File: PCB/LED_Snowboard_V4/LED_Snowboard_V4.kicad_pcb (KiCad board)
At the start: 4 copper layers, 100 x 100 mm, 114 parts, among them J1 Charge_Balance, J10 Output, J11 Micro_SD_Card_Det_Hirose_DM3AT, J12 Power Switch, J2 Bat2_Balance, J3 Bat1_Balance, J4 Bat1, J5 Bat2, J7 LED Data, J8 Sensor Input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

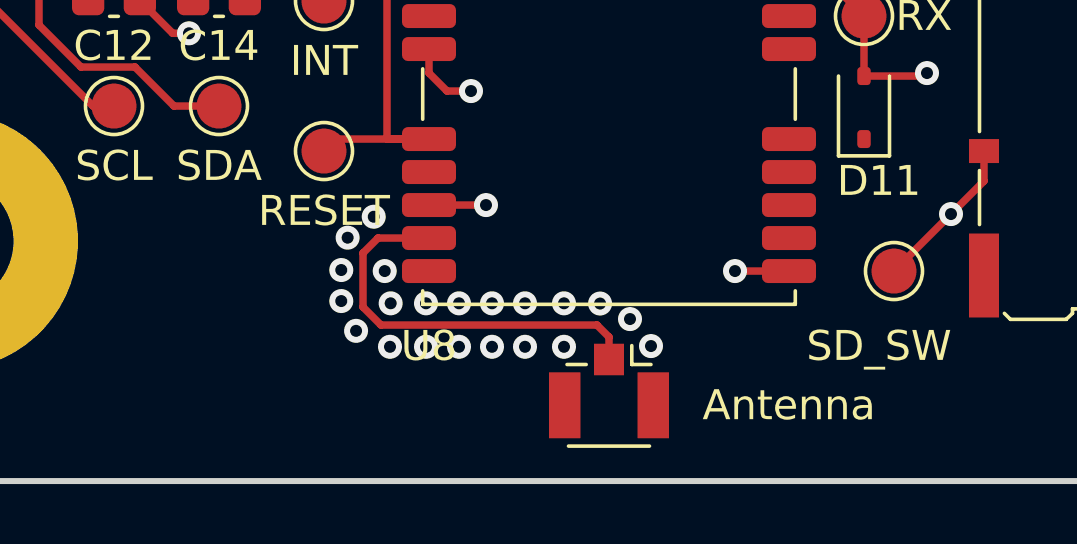
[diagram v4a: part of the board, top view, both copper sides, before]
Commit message: impedance matched antennae
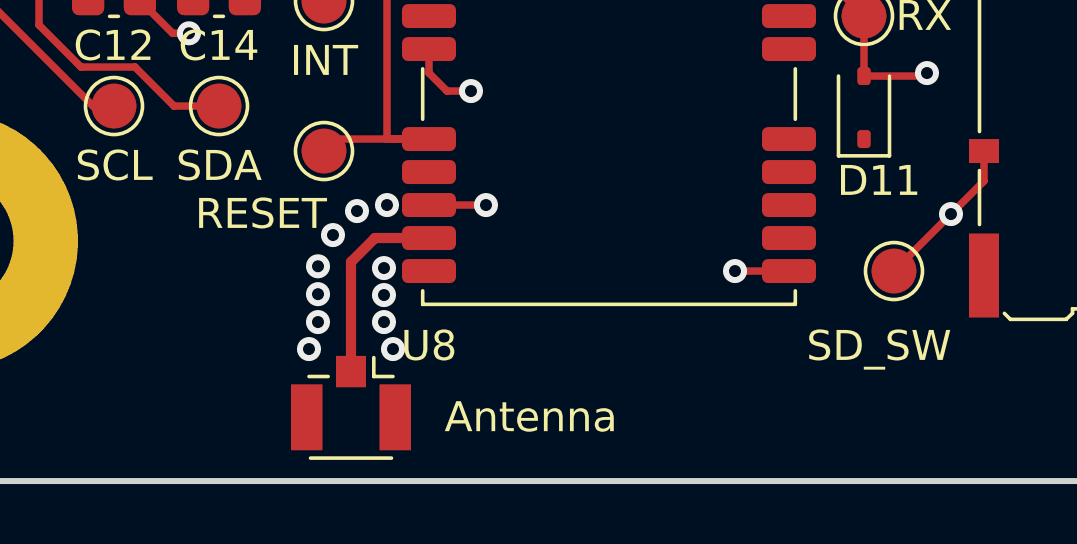
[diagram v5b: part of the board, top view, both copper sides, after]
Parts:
- moved AE1 8.61 mm to (163.4, 147.4)
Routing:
- net Net-(AE1-A): track 13.6 -> 6.58 mm
- net GND: vias 70 -> 60
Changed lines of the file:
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@@
   )
   (footprint "Connector_Coaxial:U.FL_Hirose_U.FL-R-SMT-1_Vertical" (layer "F.Cu")
-    (at 172 147 -90)
+    (at 163.4 147.4 -90)
     (descr "Hirose U.FL Coaxial https://www.hirose.com/product/en/products/U.FL/U.FL-R-SMT-1%2810%29/")
     (tags "Hirose U.FL Coaxial")
@@
         (effects (font (size 1 1) (thickness 0.15)))
     )
-    (fp_text value "RESET" (at 0 2) (layer "F.SilkS")
+    (fp_text value "RESET" (at -2.1 2.1) (layer "F.SilkS")
         (effects (font (size 1 1) (thickness 0.15)))
     )
@@
   (gr_rect (start 100 50) (end 200 150)
     (stroke (width 0.2) (type default)) (fill none) (layer "Edge.Cuts"))
-  (segment (start 166 141.9) (end 164.3 141.9) (width 0.25) (layer "F.Cu") (net 1))
-  (segment (start 171.6 144.8) (end 172 145.2) (width 0.25) (layer "F.Cu") (net 1))
-  (segment (start 164.3 141.9) (end 163.8 142.4) (width 0.25) (layer "F.Cu") (net 1))
-  (segment (start 172 145.2) (end 172 145.95) (width 0.25) (layer "F.Cu") (net 1))
-  (segment (start 163.8 144.2) (end 164.4 144.8) (width 0.25) (layer "F.Cu") (net 1))
-  (segment (start 164.4 144.8) (end 171.6 144.8) (width 0.25) (layer "F.Cu") (net 1))
-  (segment (start 163.8 142.4) (end 163.8 144.2) (width 0.25) (layer "F.Cu") (net 1))
+  (segment (start 166 141.9) (end 164.2 141.9) (width 0.3424) (layer "F.Cu") (net 1))
+  (segment (start 164.2 141.9) (end 163.4 142.7) (width 0.3424) (layer "F.Cu") (net 1))
+  (segment (start 163.4 142.7) (end 163.4 146.35) (width 0.3424) (layer "F.Cu") (net 1))
   (segment (start 155.8 113.6) (end 155.5 113.9) (width 0.25) (layer "F.Cu") (net 2))
   (segment (start 161 129.6375) (end 160.6125 129.25) (width 0.25) (layer "F.Cu") (net 2))
@@
   (segment (start 151.7 108.5) (end 151.8 108.4) (width 0.25) (layer "F.Cu") (net 2))
   (via (at 166.2 123.6) (size 0.8) (drill 0.4) (layers "F.Cu" "B.Cu") (free) (net 2))
-  (via (at 170.5 144.0755) (size 0.8) (drill 0.4) (layers "F.Cu" "B.Cu") (net 2))
   (via (at 168.2 118.4) (size 0.8) (drill 0.4) (layers "F.Cu" "B.Cu") (free) (net 2))
   (via (at 163.6 123.6) (size 0.8) (drill 0.4) (layers "F.Cu" "B.Cu") (free) (net 2))
   (via (at 168.2 117.2) (size 0.8) (drill 0.4) (layers "F.Cu" "B.Cu") (free) (net 2))
-  (via (at 167 145.5245) (size 0.8) (drill 0.4) (layers "F.Cu" "B.Cu") (net 2))
   (via (at 125 57.4) (size 0.8) (drill 0.4) (layers "F.Cu" "B.Cu") (net 2))
   (via (at 135 128.8) (size 0.8) (drill 0.4) (layers "F.Cu" "B.Cu") (free) (net 2))
   (via (at 126.3 57.4) (size 0.8) (drill 0.4) (layers "F.Cu" "B.Cu") (net 2))
   (via (at 126.3 55.7) (size 0.8) (drill 0.4) (layers "F.Cu" "B.Cu") (net 2))
-  (via (at 169.2 145.5245) (size 0.8) (drill 0.4) (layers "F.Cu" "B.Cu") (net 2))
   (via (at 127.3 65.2) (size 0.8) (drill 0.4) (layers "F.Cu" "B.Cu") (net 2))
   (via (at 161 122.6) (size 0.8) (drill 0.4) (layers "F.Cu" "B.Cu") (free) (net 2))
   (via (at 161 128.3) (size 0.8) (drill 0.4) (layers "F.Cu" "B.Cu") (net 2))
   (via (at 197.9 124.7) (size 0.8) (drill 0.4) (layers "F.Cu" "B.Cu") (net 2))
-  (via (at 165.9 144.0755) (size 0.8) (drill 0.4) (layers "F.Cu" "B.Cu") (net 2))
-  (via (at 164.722138 144.0755) (size 0.8) (drill 0.4) (layers "F.Cu" "B.Cu") (net 2))
-  (via (at 163.568797 144.993395) (size 0.8) (drill 0.4) (layers "F.Cu" "B.Cu") (net 2))
   (via (at 167.9 140.8) (size 0.8) (drill 0.4) (layers "F.Cu" "B.Cu") (net 2))
+  (via (at 162.8 141.8) (size 0.8) (drill 0.4) (layers "F.Cu" "B.Cu") (net 2))
   (via (at 126.2 65.2) (size 0.8) (drill 0.4) (layers "F.Cu" "B.Cu") (net 2))
   (via (at 126.2 62.6) (size 0.8) (drill 0.4) (layers "F.Cu" "B.Cu") (net 2))
   (via (at 159 117.2) (size 0.8) (drill 0.4) (layers "F.Cu" "B.Cu") (free) (net 2))
-  (via (at 165.9 145.5245) (size 0.8) (drill 0.4) (layers "F.Cu" "B.Cu") (net 2))
   (via (at 161 123.6) (size 0.8) (drill 0.4) (layers "F.Cu" "B.Cu") (free) (net 2))
   (via (at 126.2 63.9) (size 0.8) (drill 0.4) (layers "F.Cu" "B.Cu") (net 2))
   (via (at 121.5 144) (size 0.8) (drill 0.4) (layers "F.Cu" "B.Cu") (net 2))
+  (via (at 162.3 143.770497) (size 0.8) (drill 0.4) (layers "F.Cu" "B.Cu") (net 2))
   (via (at 159 119.6) (size 0.8) (drill 0.4) (layers "F.Cu" "B.Cu") (free) (net 2))
-  (via (at 171.70246 144.082781) (size 0.8) (drill 0.4) (layers "F.Cu" "B.Cu") (net 2))
-  (via (at 169.2 144.0755) (size 0.8) (drill 0.4) (layers "F.Cu" "B.Cu") (net 2))
   (via (at 171.6 55) (size 0.8) (drill 0.4) (layers "F.Cu" "B.Cu") (net 2))
   (via (at 163.6 122.6) (size 0.8) (drill 0.4) (layers "F.Cu" "B.Cu") (free) (net 2))
   (via (at 126.3 59) (size 0.8) (drill 0.4) (layers "F.Cu" "B.Cu") (net 2))
+  (via (at 164.8 145.6) (size 0.8) (drill 0.4) (layers "F.Cu" "B.Cu") (net 2))
   (via (at 178 127) (size 0.8) (drill 0.4) (layers "F.Cu" "B.Cu") (net 2))
   (via (at 124 131.5) (size 0.8) (drill 0.4) (layers "F.Cu" "B.Cu") (net 2))
   (via (at 168.2 121) (size 0.8) (drill 0.4) (layers "F.Cu" "B.Cu") (free) (net 2))
-  (via (at 164.7 145.5245) (size 0.8) (drill 0.4) (layers "F.Cu" "B.Cu") (net 2))
   (via (at 125.1 62.6) (size 0.8) (drill 0.4) (layers "F.Cu" "B.Cu") (net 2))
   (via (at 125.1 65.2) (size 0.8) (drill 0.4) (layers "F.Cu" "B.Cu") (net 2))
+  (via (at 162 145.6) (size 0.8) (drill 0.4) (layers "F.Cu" "B.Cu") (net 2))
+  (via (at 162.3 144.7) (size 0.8) (drill 0.4) (layers "F.Cu" "B.Cu") (net 2))
+  (via (at 162.3 142.840994) (size 0.8) (drill 0.4) (layers "F.Cu" "B.Cu") (net 2))
   (via (at 168.2 119.6) (size 0.8) (drill 0.4) (layers "F.Cu" "B.Cu") (free) (net 2))
   (via (at 127.3 62.6) (size 0.8) (drill 0.4) (layers "F.Cu" "B.Cu") (net 2))
   (via (at 159 118.4) (size 0.8) (drill 0.4) (layers "F.Cu" "B.Cu") (free) (net 2))
-  (via (at 163.0755 142.96574) (size 0.8) (drill 0.4) (layers "F.Cu" "B.Cu") (net 2))
+  (via (at 164.5 143.8) (size 0.8) (drill 0.4) (layers "F.Cu" "B.Cu") (net 2))
   (via (at 125.1 63.9) (size 0.8) (drill 0.4) (layers "F.Cu" "B.Cu") (net 2))
   (via (at 125 59) (size 0.8) (drill 0.4) (layers "F.Cu" "B.Cu") (net 2))
-  (via (at 168.1 145.5245) (size 0.8) (drill 0.4) (layers "F.Cu" "B.Cu") (net 2))
   (via (at 125 55.7) (size 0.8) (drill 0.4) (layers "F.Cu" "B.Cu") (net 2))
-  (via (at 172.7 144.6) (size 0.8) (drill 0.4) (layers "F.Cu" "B.Cu") (net 2))
   (via (at 154.4 131.8) (size 0.8) (drill 0.4) (layers "F.Cu" "B.Cu") (net 2))
-  (via (at 164.5245 143) (size 0.8) (drill 0.4) (layers "F.Cu" "B.Cu") (net 2))
   (via (at 159 121) (size 0.8) (drill 0.4) (layers "F.Cu" "B.Cu") (free) (net 2))
+  (via (at 163.6 141) (size 0.8) (drill 0.4) (layers "F.Cu" "B.Cu") (net 2))
   (via (at 127.5 55.7) (size 0.8) (drill 0.4) (layers "F.Cu" "B.Cu") (net 2))
   (via (at 127.4 59) (size 0.8) (drill 0.4) (layers "F.Cu" "B.Cu") (net 2))
@@
   (via (at 176.2 143) (size 0.8) (drill 0.4) (layers "F.Cu" "B.Cu") (net 2))
   (via (at 151.6 111.6) (size 0.8) (drill 0.4) (layers "F.Cu" "B.Cu") (free) (net 2))
-  (via (at 167 144.0755) (size 0.8) (drill 0.4) (layers "F.Cu" "B.Cu") (net 2))
-  (via (at 164.157914 141.189568) (size 0.8) (drill 0.4) (layers "F.Cu" "B.Cu") (net 2))
-  (via (at 173.4 145.5) (size 0.8) (drill 0.4) (layers "F.Cu" "B.Cu") (net 2))
+  (via (at 164.6 140.8) (size 0.8) (drill 0.4) (layers "F.Cu" "B.Cu") (net 2))
   (via (at 166.2 122.6) (size 0.8) (drill 0.4) (layers "F.Cu" "B.Cu") (free) (net 2))
   (via (at 140.9 135.9) (size 0.8) (drill 0.4) (layers "F.Cu" "B.Cu") (net 2))
-  (via (at 163.0755 144) (size 0.8) (drill 0.4) (layers "F.Cu" "B.Cu") (net 2))
-  (via (at 163.287701 141.887701) (size 0.8) (drill 0.4) (layers "F.Cu" "B.Cu") (net 2))
+  (via (at 164.5 142.9) (size 0.8) (drill 0.4) (layers "F.Cu" "B.Cu") (net 2))
   (via (at 184.4 124.5) (size 0.8) (drill 0.4) (layers "F.Cu" "B.Cu") (net 2))
   (via (at 127.3 63.9) (size 0.8) (drill 0.4) (layers "F.Cu" "B.Cu") (net 2))
@@
   (via (at 151.7 131.8) (size 0.8) (drill 0.4) (layers "F.Cu" "B.Cu") (net 2))
   (via (at 150.6 127.5) (size 0.8) (drill 0.4) (layers "F.Cu" "B.Cu") (net 2))
-  (via (at 168.1 144.0755) (size 0.8) (drill 0.4) (layers "F.Cu" "B.Cu") (net 2))
-  (via (at 170.5 145.5245) (size 0.8) (drill 0.4) (layers "F.Cu" "B.Cu") (net 2))
+  (via (at 164.5 144.7) (size 0.8) (drill 0.4) (layers "F.Cu" "B.Cu") (net 2))
   (segment (start 167.4 137) (end 166.6 137) (width 0.25) (layer "F.Cu") (net 3))
   (segment (start 141.45 112.65) (end 141.6 112.8) (width 1) (layer "F.Cu") (net 3))
